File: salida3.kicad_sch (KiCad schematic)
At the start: 0 parts

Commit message: add salidas separadas 4,5,6
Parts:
- added ? (x5): (no value), symbol Device:R
- added ?: (no value), symbol Isolator:ILD74
- added ?: (no value), symbol Transistor_FET:FQP27P06
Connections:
- new net: ?.1, ?.1, ?.7
- new net: ?.1 (G), ?.2
- new net: ?.1, ?.2
- new net 3L: ?.2, ?.2 (D)
- new net GND: ?.2, ?.2
- new net IO05: ?.1, ?.1
- new net M3: ?.1, ?.8
- new net Q3: ?.2, ?.3 (S)
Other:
- note added: "Salida Q3"

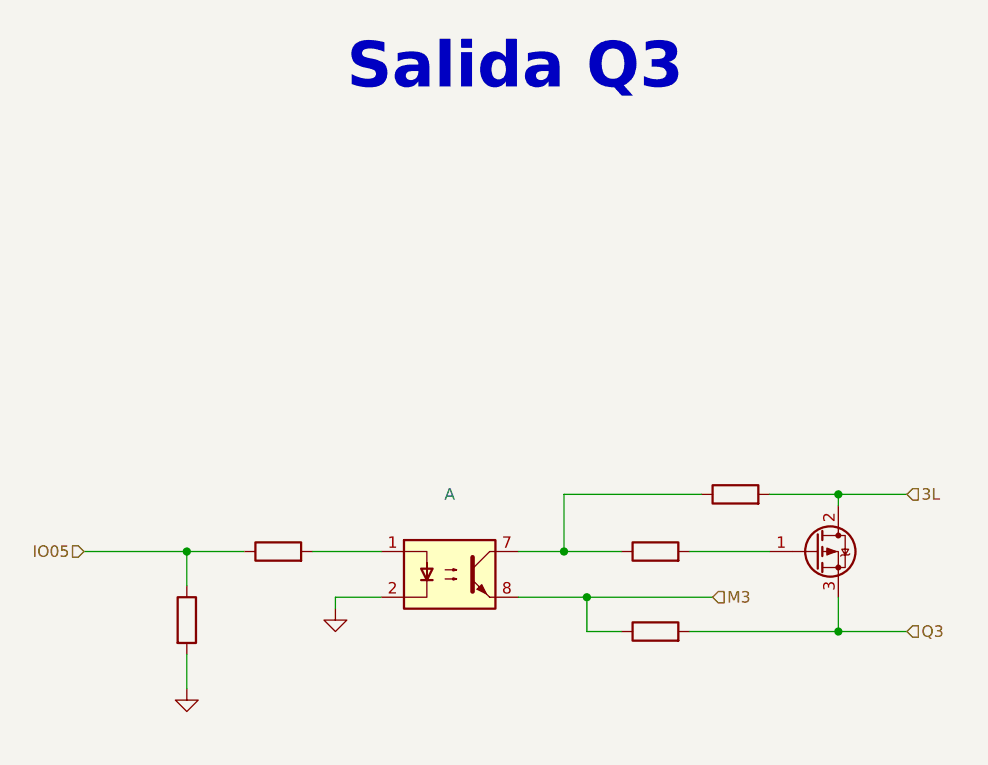
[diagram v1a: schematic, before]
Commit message: add entradas separadas
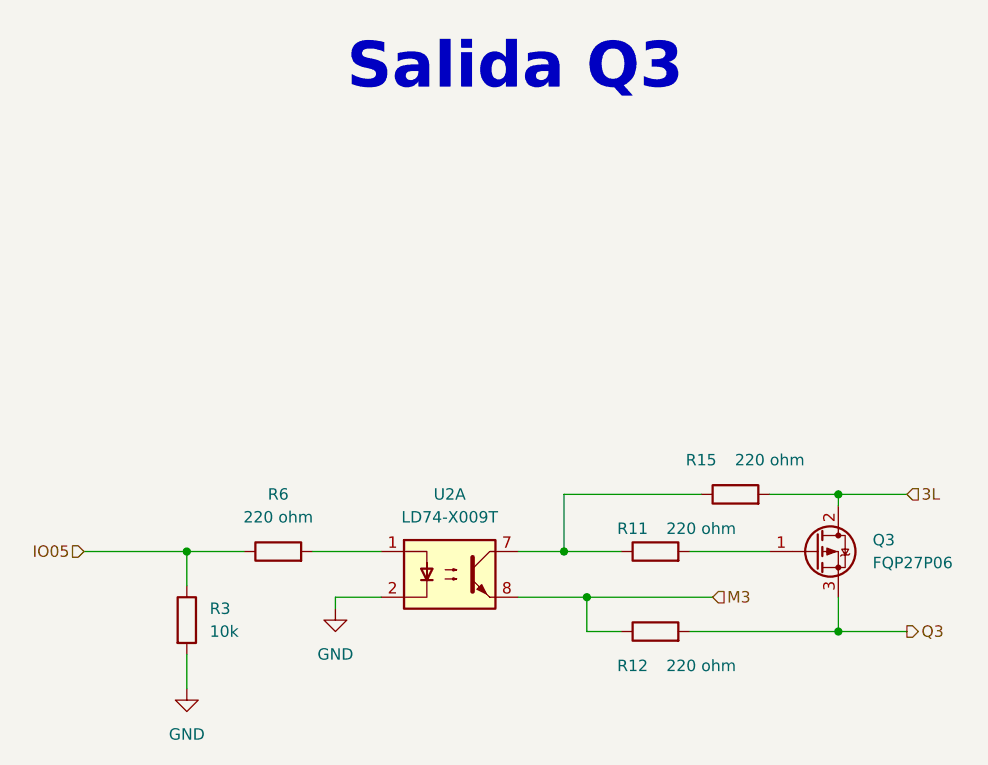
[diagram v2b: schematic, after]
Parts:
- Q3: renamed from ?; value (none) -> FQP27P06; footprint (none) -> Package_TO_SOT_SMD:TO-252-3_TabPin2
- R11, R12, R15: renamed from ?; value (none) -> 220 ohm; footprint (none) -> Resistor_SMD:R_0603_1608Metric
- R3: renamed from ?; value (none) -> 10k; footprint (none) -> Resistor_SMD:R_0603_1608Metric
- R6: renamed from ?; value (none) -> 220 ohm; footprint (none) -> Resistor_SMD:R_0603_1608Metric_Pad0.98x0.95mm_HandSolder
- U2: renamed from ?; value (none) -> LD74-X009T; footprint (none) -> Package_DIP:DIP-8_W8.89mm_SMDSocket_LongPads
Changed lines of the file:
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@@
-(kicad_sch (version 20220929) (generator eeschema)
+(kicad_sch (version 20221004) (generator eeschema)
   (paper "A4" portrait)
+  (title_block
+    (rev "José Luis Laica")
+  )
   (junction (at 107.95 132.08) (diameter 0) (color 0 0 0 0)
   )
@@
     (effects (font (size 1.27 1.27)) (justify left))
   )
-  (hierarchical_label "Q3" (shape input) (at 146.05 140.97 0) (fields_autoplaced)
+  (hierarchical_label "Q3" (shape output) (at 146.05 140.97 0) (fields_autoplaced)
     (effects (font (size 1.27 1.27)) (justify left))
   )
@@
   (symbol (lib_id "Device:R") (at 66.04 139.7 0) (unit 1)
     (in_bom yes) (on_board yes) (dnp no) (fields_autoplaced)
-    (default_instance (reference "") (unit 1) (value "") (footprint ""))
-    (property "Reference" "" (at 68.58 138.4299 0)
-      (effects (font (size 1.27 1.27)) (justify left))
-    )
-    (property "Value" "" (at 68.58 140.9699 0)
-      (effects (font (size 1.27 1.27)) (justify left))
-    )
-    (property "Footprint" "" (at 64.262 139.7 90)
+    (property "Reference" "R3" (at 68.58 138.4299 0)
+      (effects (font (size 1.27 1.27)) (justify left))
+    )
+    (property "Value" "10k" (at 68.58 140.9699 0)
+      (effects (font (size 1.27 1.27)) (justify left))
+    )
+    (property "Footprint" "Resistor_SMD:R_0603_1608Metric" (at 64.262 139.7 90)
       (effects (font (size 1.27 1.27)) hide)
     )
@@
     (pin "1")
     (pin "2")
+    (instances
+      (project "PLC 32 V2"
+        (path "/d17a54f1-6eda-453f-95e1-42a53b02a1c3/e0987795-0f8d-4564-9094-c23cc01406e8"
+          (reference "R3") (unit 1) (value "10k") (footprint "Resistor_SMD:R_0603_1608Metric")
+        )
+      )
+    )
   )
   (symbol (lib_id "power:GND") (at 66.04 147.32 0) (unit 1)
     (in_bom yes) (on_board yes) (dnp no) (fields_autoplaced)
-    (default_instance (reference "") (unit 1) (value "") (footprint ""))
-    (property "Reference" "" (at 66.04 153.67 0)
-      (effects (font (size 1.27 1.27)) hide)
-    )
-    (property "Value" "" (at 66.04 152.4 0)
+    (property "Reference" "#PWR07" (at 66.04 153.67 0)
+      (effects (font (size 1.27 1.27)) hide)
+    )
+    (property "Value" "GND" (at 66.04 152.4 0)
       (effects (font (size 1.27 1.27)))
     )
@@
     )
     (pin "1")
+    (instances
+      (project "PLC 32 V2"
+        (path "/d17a54f1-6eda-453f-95e1-42a53b02a1c3/e0987795-0f8d-4564-9094-c23cc01406e8"
+          (reference "#PWR07") (unit 1) (value "GND") (footprint "")
+        )
+      )
+    )
   )
   (symbol (lib_id "Device:R") (at 127 125.73 90) (unit 1)
     (in_bom yes) (on_board yes) (dnp no)
-    (default_instance (reference "") (unit 1) (value "") (footprint ""))
-    (property "Reference" "" (at 123.19 121.92 90)
-      (effects (font (size 1.27 1.27)))
-    )
-    (property "Value" "" (at 130.81 121.92 90)
-      (effects (font (size 1.27 1.27)))
-    )
-    (property "Footprint" "" (at 127 127.508 90)
+    (property "Reference" "R15" (at 123.19 121.92 90)
+      (effects (font (size 1.27 1.27)))
+    )
+    (property "Value" "220 ohm" (at 130.81 121.92 90)
+      (effects (font (size 1.27 1.27)))
+    )
+    (property "Footprint" "Resistor_SMD:R_0603_1608Metric" (at 127 127.508 90)
       (effects (font (size 1.27 1.27)) hide)
     )
@@
     (pin "1")
     (pin "2")
+    (instances
+      (project "PLC 32 V2"
+        (path "/d17a54f1-6eda-453f-95e1-42a53b02a1c3/e0987795-0f8d-4564-9094-c23cc01406e8"
+          (reference "R15") (unit 1) (value "220 ohm") (footprint "Resistor_SMD:R_0603_1608Metric")
+        )
+      )
+    )
   )
   (symbol (lib_id "Device:R") (at 118.11 140.97 90) (unit 1)
     (in_bom yes) (on_board yes) (dnp no)
-    (default_instance (reference "") (unit 1) (value "") (footprint ""))
-    (property "Reference" "" (at 115.57 144.78 90)
-      (effects (font (size 1.27 1.27)))
-    )
-    (property "Value" "" (at 123.19 144.78 90)
-      (effects (font (size 1.27 1.27)))
-    )
-    (property "Footprint" "" (at 118.11 142.748 90)
+    (property "Reference" "R12" (at 115.57 144.78 90)
+      (effects (font (size 1.27 1.27)))
+    )
+    (property "Value" "220 ohm" (at 123.19 144.78 90)
+      (effects (font (size 1.27 1.27)))
+    )
+    (property "Footprint" "Resistor_SMD:R_0603_1608Metric" (at 118.11 142.748 90)
       (effects (font (size 1.27 1.27)) hide)
     )
@@
     (pin "1")
     (pin "2")
+    (instances
+      (project "PLC 32 V2"
+        (path "/d17a54f1-6eda-453f-95e1-42a53b02a1c3/e0987795-0f8d-4564-9094-c23cc01406e8"
+          (reference "R12") (unit 1) (value "220 ohm") (footprint "Resistor_SMD:R_0603_1608Metric")
+        )
+      )
+    )
   )
   (symbol (lib_id "power:GND") (at 82.55 138.43 0) (unit 1)
     (in_bom yes) (on_board yes) (dnp no) (fields_autoplaced)
-    (default_instance (reference "") (unit 1) (value "") (footprint ""))
-    (property "Reference" "" (at 82.55 144.78 0)
-      (effects (font (size 1.27 1.27)) hide)
-    )
-    (property "Value" "" (at 82.55 143.51 0)
+    (property "Reference" "#PWR010" (at 82.55 144.78 0)
+      (effects (font (size 1.27 1.27)) hide)
+    )
+    (property "Value" "GND" (at 82.55 143.51 0)
       (effects (font (size 1.27 1.27)))
     )
@@
     )
     (pin "1")
+    (instances
+      (project "PLC 32 V2"
+        (path "/d17a54f1-6eda-453f-95e1-42a53b02a1c3/e0987795-0f8d-4564-9094-c23cc01406e8"
+          (reference "#PWR010") (unit 1) (value "GND") (footprint "")
+        )
+      )
+    )
   )
   (symbol (lib_id "Device:R") (at 118.11 132.08 90) (unit 1)
     (in_bom yes) (on_board yes) (dnp no)
-    (default_instance (reference "") (unit 1) (value "") (footprint ""))
-    (property "Reference" "" (at 115.57 129.54 90)
-      (effects (font (size 1.27 1.27)))
-    )
-    (property "Value" "" (at 123.19 129.54 90)
-      (effects (font (size 1.27 1.27)))
-    )
-    (property "Footprint" "" (at 118.11 133.858 90)
+    (property "Reference" "R11" (at 115.57 129.54 90)
+      (effects (font (size 1.27 1.27)))
+    )
+    (property "Value" "220 ohm" (at 123.19 129.54 90)
+      (effects (font (size 1.27 1.27)))
+    )
+    (property "Footprint" "Resistor_SMD:R_0603_1608Metric" (at 118.11 133.858 90)
       (effects (font (size 1.27 1.27)) hide)
     )
@@
     (pin "1")
     (pin "2")
+    (instances
+      (project "PLC 32 V2"
+        (path "/d17a54f1-6eda-453f-95e1-42a53b02a1c3/e0987795-0f8d-4564-9094-c23cc01406e8"
+          (reference "R11") (unit 1) (value "220 ohm") (footprint "Resistor_SMD:R_0603_1608Metric")
+        )
+      )
+    )
   )
   (symbol (lib_id "Device:R") (at 76.2 132.08 90) (unit 1)
     (in_bom yes) (on_board yes) (dnp no) (fields_autoplaced)
-    (default_instance (reference "") (unit 1) (value "") (footprint ""))
-    (property "Reference" "" (at 76.2 125.73 90)
-      (effects (font (size 1.27 1.27)))
-    )
-    (property "Value" "" (at 76.2 128.27 90)
-      (effects (font (size 1.27 1.27)))
-    )
-    (property "Footprint" "" (at 76.2 133.858 90)
+    (property "Reference" "R6" (at 76.2 125.73 90)
+      (effects (font (size 1.27 1.27)))
+    )
+    (property "Value" "220 ohm" (at 76.2 128.27 90)
+      (effects (font (size 1.27 1.27)))
+    )
+    (property "Footprint" "Resistor_SMD:R_0603_1608Metric_Pad0.98x0.95mm_HandSolder" (at 76.2 133.858 90)
       (effects (font (size 1.27 1.27)) hide)
     )
@@
     (pin "1")
     (pin "2")
+    (instances
+      (project "PLC 32 V2"
+        (path "/d17a54f1-6eda-453f-95e1-42a53b02a1c3/e0987795-0f8d-4564-9094-c23cc01406e8"
+          (reference "R6") (unit 1) (value "220 ohm") (footprint "Resistor_SMD:R_0603_1608Metric_Pad0.98x0.95mm_HandSolder")
+        )
+      )
+    )
   )
   (symbol (lib_id "Isolator:ILD74") (at 95.25 134.62 0) (unit 1)
     (in_bom yes) (on_board yes) (dnp no) (fields_autoplaced)
-    (default_instance (reference "") (unit 1) (value "") (footprint ""))
-    (property "Reference" "" (at 95.25 125.73 0)
-      (effects (font (size 1.27 1.27)))
-    )
-    (property "Value" "" (at 95.25 128.27 0)
-      (effects (font (size 1.27 1.27)))
-    )
-    (property "Footprint" "" (at 90.17 139.7 0)
+    (property "Reference" "U2" (at 95.25 125.73 0)
+      (effects (font (size 1.27 1.27)))
+    )
+    (property "Value" "LD74-X009T" (at 95.25 128.27 0)
+      (effects (font (size 1.27 1.27)))
+    )
+    (property "Footprint" "Package_DIP:DIP-8_W8.89mm_SMDSocket_LongPads" (at 90.17 139.7 0)
       (effects (font (size 1.27 1.27) italic) (justify left) hide)
     )
@@
     (pin "5")
     (pin "6")
+    (instances
+      (project "PLC 32 V2"
+        (path "/d17a54f1-6eda-453f-95e1-42a53b02a1c3/e0987795-0f8d-4564-9094-c23cc01406e8"
+          (reference "U2") (unit 1) (value "LD74-X009T") (footprint "Package_DIP:DIP-8_W8.89mm_SMDSocket_LongPads")
+        )
+      )
+    )
   )
   (symbol (lib_id "Transistor_FET:FQP27P06") (at 135.89 132.08 0) (unit 1)
     (in_bom yes) (on_board yes) (dnp no) (fields_autoplaced)
-    (default_instance (reference "") (unit 1) (value "") (footprint ""))
-    (property "Reference" "" (at 142.24 130.8099 0)
-      (effects (font (size 1.27 1.27)) (justify left))
-    )
-    (property "Value" "" (at 142.24 133.3499 0)
-      (effects (font (size 1.27 1.27)) (justify left))
-    )
-    (property "Footprint" "" (at 140.97 133.985 0)
+    (property "Reference" "Q3" (at 142.24 130.8099 0)
+      (effects (font (size 1.27 1.27)) (justify left))
+    )
+    (property "Value" "FQP27P06" (at 142.24 133.3499 0)
+      (effects (font (size 1.27 1.27)) (justify left))
+    )
+    (property "Footprint" "Package_TO_SOT_SMD:TO-252-3_TabPin2" (at 140.97 133.985 0)
       (effects (font (size 1.27 1.27) italic) (justify left) hide)
     )
@@
     (pin "2")
     (pin "3")
+    (instances
+      (project "PLC 32 V2"
+        (path "/d17a54f1-6eda-453f-95e1-42a53b02a1c3/e0987795-0f8d-4564-9094-c23cc01406e8"
+          (reference "Q3") (unit 1) (value "FQP27P06") (footprint "Package_TO_SOT_SMD:TO-252-3_TabPin2")
+        )
+      )
+    )
   )
 )

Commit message: input/output separadas
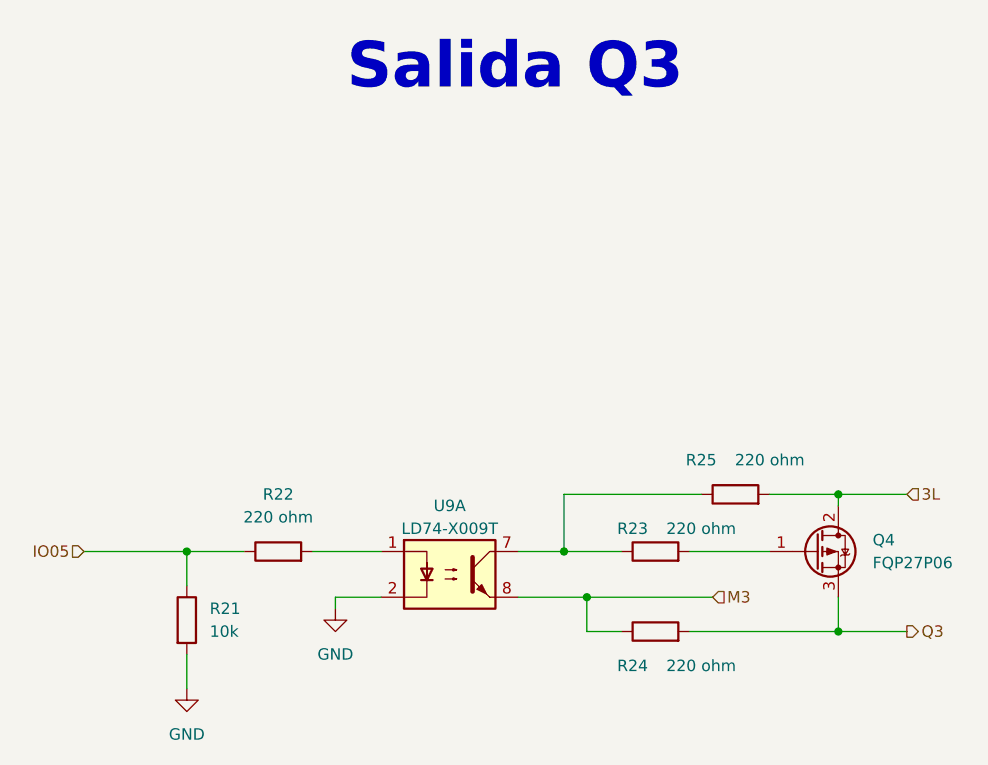
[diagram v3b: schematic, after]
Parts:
- renumbered Q3 to Q4, R3 to R21, R6 to R22, R11 to R23, R12 to R24, R15 to R25, U2 to U9
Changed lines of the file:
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@@
   (paper "A4" portrait)
   (title_block
+    (date "2022-10-09")
     (rev "José Luis Laica")
   )
@@
   (symbol (lib_id "Device:R") (at 66.04 139.7 0) (unit 1)
     (in_bom yes) (on_board yes) (dnp no) (fields_autoplaced)
-    (property "Reference" "R3" (at 68.58 138.4299 0)
+    (property "Reference" "R21" (at 68.58 138.4299 0)
       (effects (font (size 1.27 1.27)) (justify left))
     )
@@
       (project "PLC 32 V2"
         (path "/d17a54f1-6eda-453f-95e1-42a53b02a1c3/e0987795-0f8d-4564-9094-c23cc01406e8"
-          (reference "R3") (unit 1) (value "10k") (footprint "Resistor_SMD:R_0603_1608Metric")
+          (reference "R21") (unit 1) (value "10k") (footprint "Resistor_SMD:R_0603_1608Metric")
         )
       )
@@
   (symbol (lib_id "power:GND") (at 66.04 147.32 0) (unit 1)
     (in_bom yes) (on_board yes) (dnp no) (fields_autoplaced)
-    (property "Reference" "#PWR07" (at 66.04 153.67 0)
+    (property "Reference" "#PWR016" (at 66.04 153.67 0)
       (effects (font (size 1.27 1.27)) hide)
     )
@@
       (project "PLC 32 V2"
         (path "/d17a54f1-6eda-453f-95e1-42a53b02a1c3/e0987795-0f8d-4564-9094-c23cc01406e8"
-          (reference "#PWR07") (unit 1) (value "GND") (footprint "")
+          (reference "#PWR016") (unit 1) (value "GND") (footprint "")
         )
       )
@@
   (symbol (lib_id "Device:R") (at 127 125.73 90) (unit 1)
     (in_bom yes) (on_board yes) (dnp no)
-    (property "Reference" "R15" (at 123.19 121.92 90)
+    (property "Reference" "R25" (at 123.19 121.92 90)
       (effects (font (size 1.27 1.27)))
     )
@@
       (project "PLC 32 V2"
         (path "/d17a54f1-6eda-453f-95e1-42a53b02a1c3/e0987795-0f8d-4564-9094-c23cc01406e8"
-          (reference "R15") (unit 1) (value "220 ohm") (footprint "Resistor_SMD:R_0603_1608Metric")
+          (reference "R25") (unit 1) (value "220 ohm") (footprint "Resistor_SMD:R_0603_1608Metric")
         )
       )
@@
   (symbol (lib_id "Device:R") (at 118.11 140.97 90) (unit 1)
     (in_bom yes) (on_board yes) (dnp no)
-    (property "Reference" "R12" (at 115.57 144.78 90)
+    (property "Reference" "R24" (at 115.57 144.78 90)
       (effects (font (size 1.27 1.27)))
     )
@@
       (project "PLC 32 V2"
         (path "/d17a54f1-6eda-453f-95e1-42a53b02a1c3/e0987795-0f8d-4564-9094-c23cc01406e8"
-          (reference "R12") (unit 1) (value "220 ohm") (footprint "Resistor_SMD:R_0603_1608Metric")
+          (reference "R24") (unit 1) (value "220 ohm") (footprint "Resistor_SMD:R_0603_1608Metric")
         )
       )
@@
   (symbol (lib_id "power:GND") (at 82.55 138.43 0) (unit 1)
     (in_bom yes) (on_board yes) (dnp no) (fields_autoplaced)
-    (property "Reference" "#PWR010" (at 82.55 144.78 0)
+    (property "Reference" "#PWR017" (at 82.55 144.78 0)
       (effects (font (size 1.27 1.27)) hide)
     )
@@
       (project "PLC 32 V2"
         (path "/d17a54f1-6eda-453f-95e1-42a53b02a1c3/e0987795-0f8d-4564-9094-c23cc01406e8"
-          (reference "#PWR010") (unit 1) (value "GND") (footprint "")
+          (reference "#PWR017") (unit 1) (value "GND") (footprint "")
         )
       )
@@
   (symbol (lib_id "Device:R") (at 118.11 132.08 90) (unit 1)
     (in_bom yes) (on_board yes) (dnp no)
-    (property "Reference" "R11" (at 115.57 129.54 90)
+    (property "Reference" "R23" (at 115.57 129.54 90)
       (effects (font (size 1.27 1.27)))
     )
@@
       (project "PLC 32 V2"
         (path "/d17a54f1-6eda-453f-95e1-42a53b02a1c3/e0987795-0f8d-4564-9094-c23cc01406e8"
-          (reference "R11") (unit 1) (value "220 ohm") (footprint "Resistor_SMD:R_0603_1608Metric")
+          (reference "R23") (unit 1) (value "220 ohm") (footprint "Resistor_SMD:R_0603_1608Metric")
         )
       )
@@
   (symbol (lib_id "Device:R") (at 76.2 132.08 90) (unit 1)
     (in_bom yes) (on_board yes) (dnp no) (fields_autoplaced)
-    (property "Reference" "R6" (at 76.2 125.73 90)
+    (property "Reference" "R22" (at 76.2 125.73 90)
       (effects (font (size 1.27 1.27)))
     )
@@
       (project "PLC 32 V2"
         (path "/d17a54f1-6eda-453f-95e1-42a53b02a1c3/e0987795-0f8d-4564-9094-c23cc01406e8"
-          (reference "R6") (unit 1) (value "220 ohm") (footprint "Resistor_SMD:R_0603_1608Metric_Pad0.98x0.95mm_HandSolder")
+          (reference "R22") (unit 1) (value "220 ohm") (footprint "Resistor_SMD:R_0603_1608Metric_Pad0.98x0.95mm_HandSolder")
         )
       )
@@
   (symbol (lib_id "Isolator:ILD74") (at 95.25 134.62 0) (unit 1)
     (in_bom yes) (on_board yes) (dnp no) (fields_autoplaced)
-    (property "Reference" "U2" (at 95.25 125.73 0)
-      (effects (font (size 1.27 1.27)))
-    )
-    (property "Value" "LD74-X009T" (at 95.25 128.27 0)
+    (property "Reference" "U9" (at 95.25 127 0)
+      (effects (font (size 1.27 1.27)))
+    )
+    (property "Value" "LD74-X009T" (at 95.25 129.54 0)
       (effects (font (size 1.27 1.27)))
     )
@@
       (project "PLC 32 V2"
         (path "/d17a54f1-6eda-453f-95e1-42a53b02a1c3/e0987795-0f8d-4564-9094-c23cc01406e8"
-          (reference "U2") (unit 1) (value "LD74-X009T") (footprint "Package_DIP:DIP-8_W8.89mm_SMDSocket_LongPads")
+          (reference "U9") (unit 1) (value "LD74-X009T") (footprint "Package_DIP:DIP-8_W8.89mm_SMDSocket_LongPads")
         )
       )
@@
   (symbol (lib_id "Transistor_FET:FQP27P06") (at 135.89 132.08 0) (unit 1)
     (in_bom yes) (on_board yes) (dnp no) (fields_autoplaced)
-    (property "Reference" "Q3" (at 142.24 130.8099 0)
+    (property "Reference" "Q4" (at 142.24 130.8099 0)
       (effects (font (size 1.27 1.27)) (justify left))
     )
@@
       (project "PLC 32 V2"
         (path "/d17a54f1-6eda-453f-95e1-42a53b02a1c3/e0987795-0f8d-4564-9094-c23cc01406e8"
-          (reference "Q3") (unit 1) (value "FQP27P06") (footprint "Package_TO_SOT_SMD:TO-252-3_TabPin2")
-        )
-      )
+          (reference "Q4") (unit 1) (value "FQP27P06") (footprint "Package_TO_SOT_SMD:TO-252-3_TabPin2")
+        )
+      )
